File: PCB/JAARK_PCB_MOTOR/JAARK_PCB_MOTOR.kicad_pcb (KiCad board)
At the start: 2 copper layers, 1 part, among them IC1 TPS564242DRLR

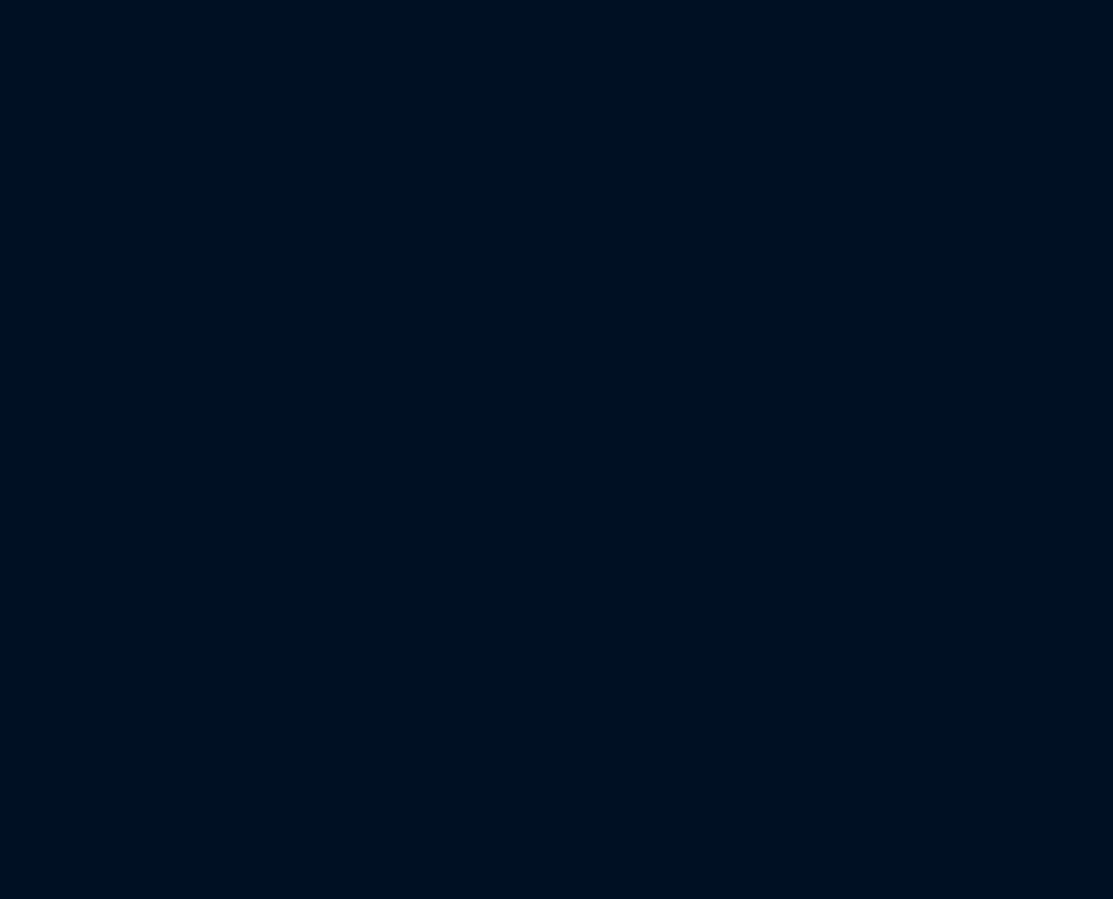
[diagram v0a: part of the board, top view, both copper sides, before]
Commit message: Organizing libraries in the local folder.
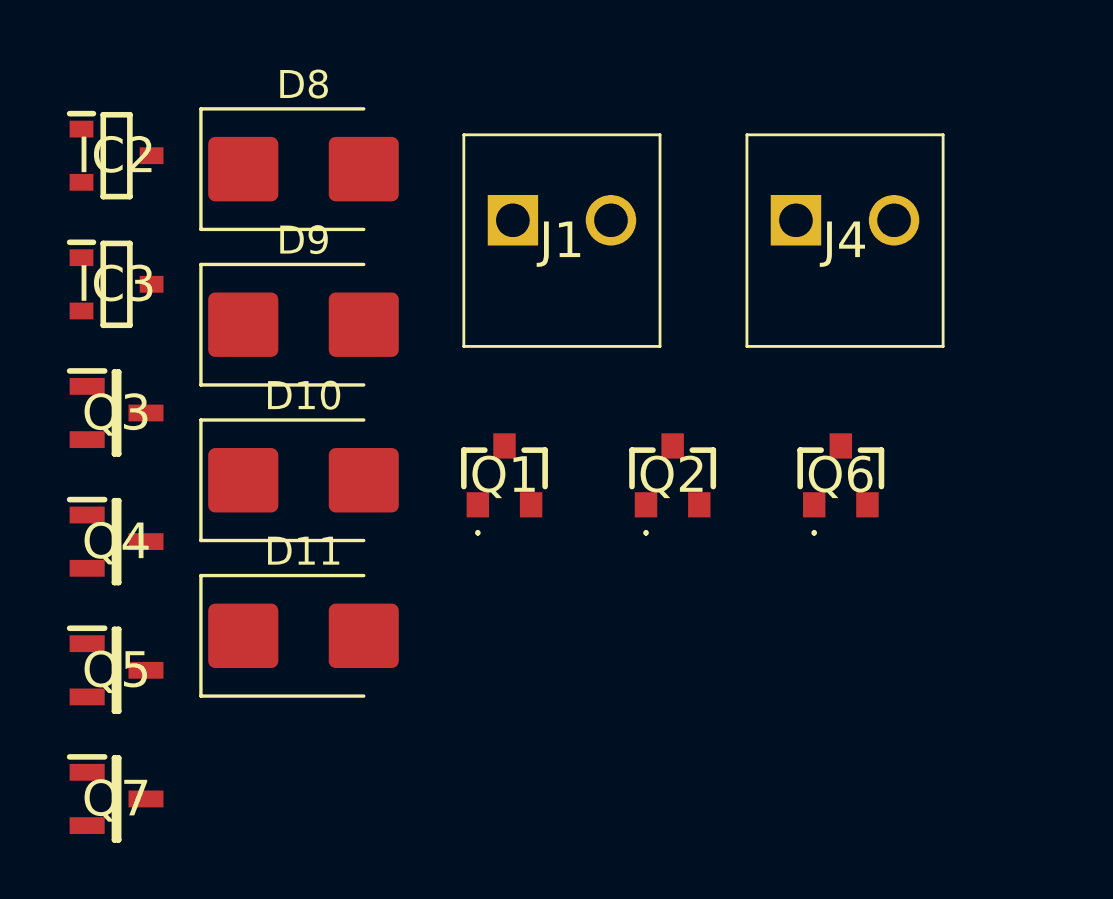
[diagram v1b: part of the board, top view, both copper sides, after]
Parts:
- added D10: S2JTR, Diode_SMD:D_SMB, F.Cu at (66.9, 59.3)
- added D11: S2JTR, Diode_SMD:D_SMB, F.Cu at (66.9, 64.8)
- added D8: S2JTR, Diode_SMD:D_SMB, F.Cu at (66.9, 48.2)
- added D9: S2JTR, Diode_SMD:D_SMB, F.Cu at (66.9, 53.8)
- added IC2: PJA3404_R1_00001, JAARK_lib:SOT95P240X110-3N, F.Cu at (60.2, 47.7)
- added IC3: PJA3404_R1_00001, JAARK_lib:SOT95P240X110-3N, F.Cu at (60.2, 52.3)
- added J1: dc=12, JAARK_lib:1984617, F.Cu at (74.3, 50.0)
- added J4: ~, JAARK_lib:1984617, F.Cu at (84.5, 50.0)
- added Q1: SSM3J334RLF, JAARK_lib:2SC2712GRLF, F.Cu at (74.0, 59.1)
- added Q2: SSM3J334RLF, JAARK_lib:2SC2712GRLF, F.Cu at (80.0, 59.1)
- added Q3: FMMT619TA, JAARK_lib:SOT95P237X112-3N, F.Cu at (60.2, 56.9)
- added Q4: FMMT619TA, JAARK_lib:SOT95P237X112-3N, F.Cu at (60.2, 61.5)
- added Q5: FMMT619TA, JAARK_lib:SOT95P237X112-3N, F.Cu at (60.2, 66.1)
- added Q6: SSM3J334RLF, JAARK_lib:2SC2712GRLF, F.Cu at (86.0, 59.1)
- added Q7: FMMT619TA, JAARK_lib:SOT95P237X112-3N, F.Cu at (60.2, 70.7)
- IC1: footprint SSys_Footprints:SOTFL50P160X60-6N -> JAARK_lib:SOTFL50P160X60-6N

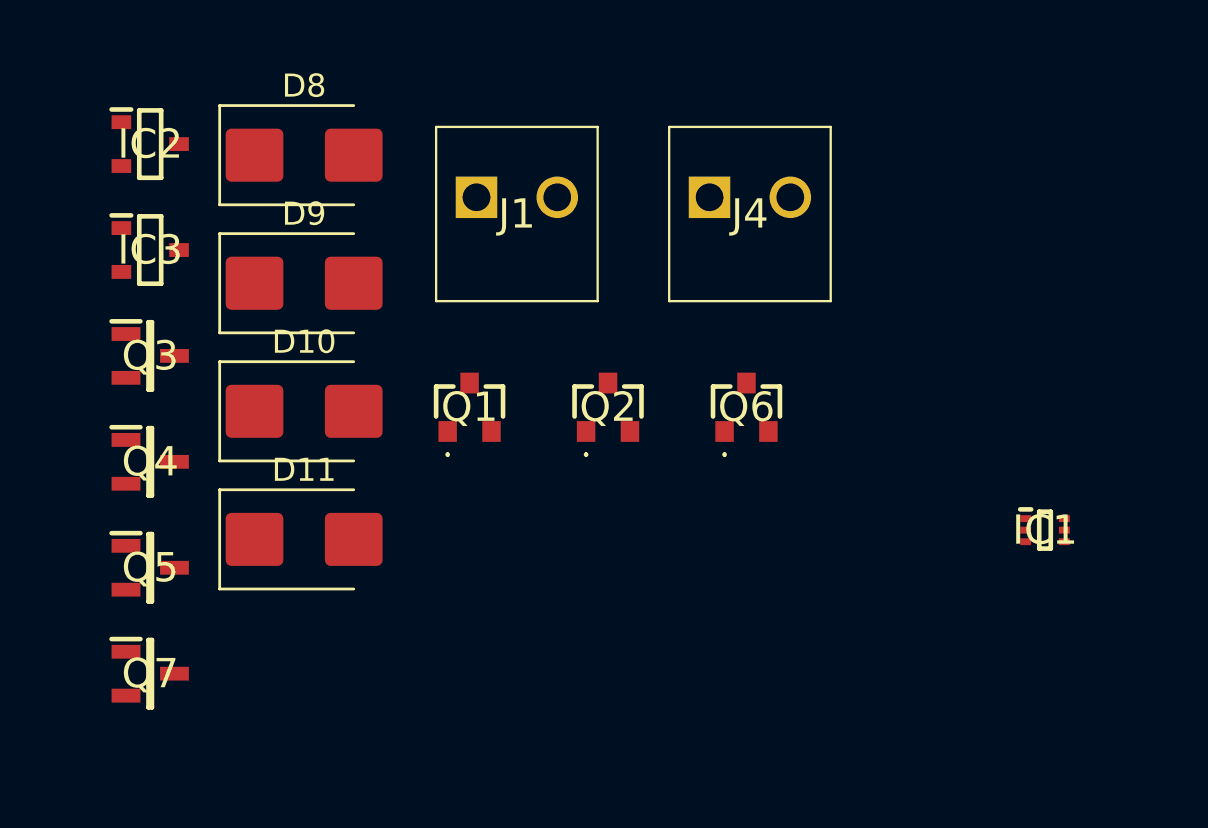
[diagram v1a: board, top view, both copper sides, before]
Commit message: Motor driver recreation, appended footprints to lots of R,L,C elements
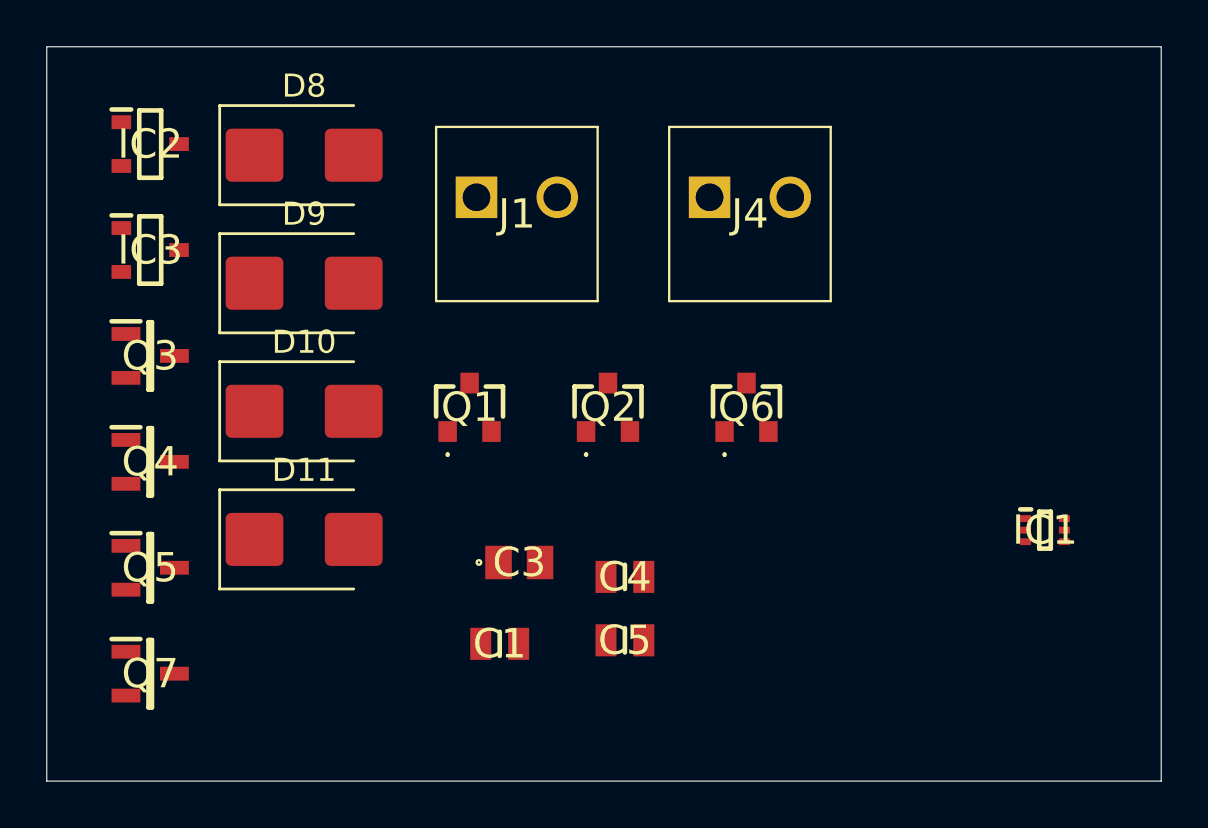
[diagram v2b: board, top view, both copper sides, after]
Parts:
- added C1: 22uF, JAARK_lib:CAPC2012X95N, F.Cu at (75.4, 69.4)
- added C3: 0.1uF, JAARK_lib:C0805, F.Cu at (76.2, 65.8)
- added C4: 22uF, JAARK_lib:CAPC2012X95N, F.Cu at (80.8, 66.5)
- added C5: 22uF, JAARK_lib:CAPC2012X95N, F.Cu at (80.8, 69.2)
- IC2, IC3: footprint JAARK_lib:SOT95P240X110-3N -> SSys_Footprints:SOT95P240X110-3N
- J1, J4: footprint JAARK_lib:1984617 -> SSys_Footprints:1984617
- Q1, Q2, Q6: footprint JAARK_lib:2SC2712GRLF -> SSys_Footprints:2SC2712GRLF
- Q3, Q4, Q5, Q7: footprint JAARK_lib:SOT95P237X112-3N -> SSys_Footprints:SOT95P237X112-3N
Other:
- board outline added: 48.3 x 31.8 mm

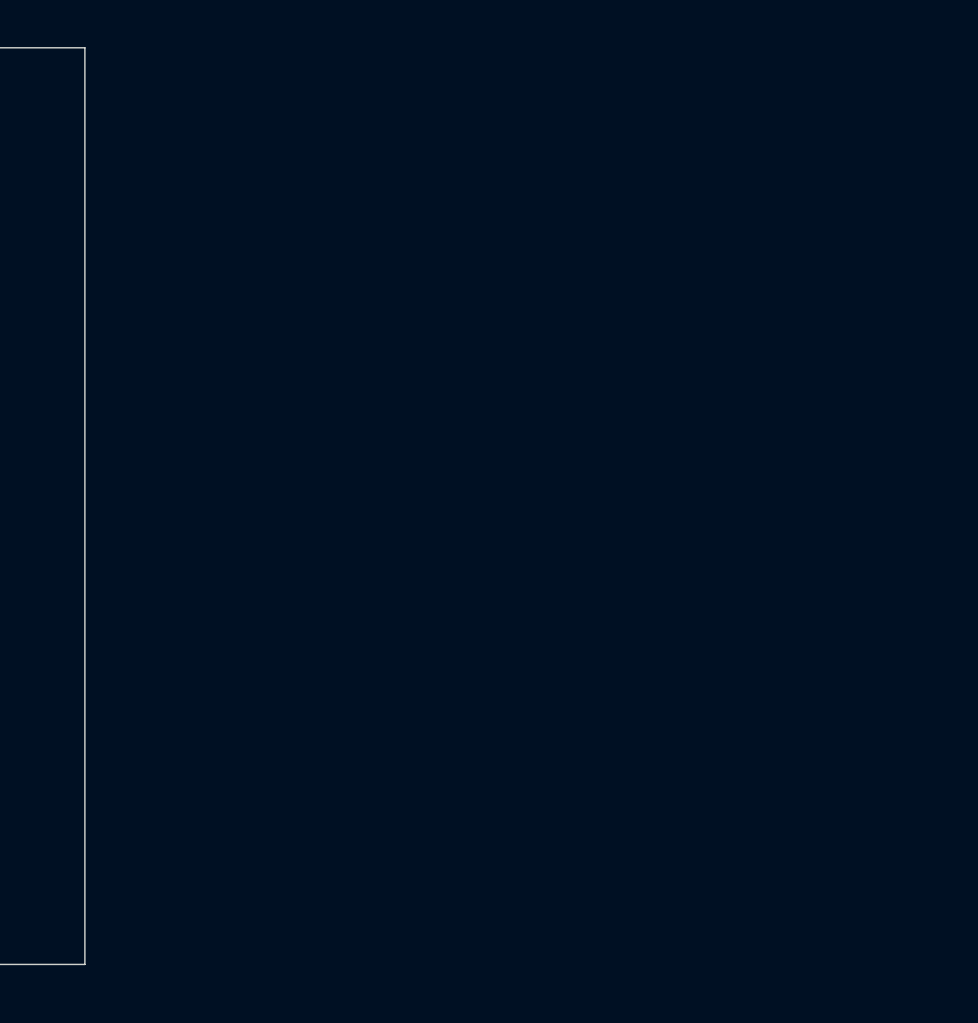
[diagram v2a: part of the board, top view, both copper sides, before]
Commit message: Fixed footprints for sharing
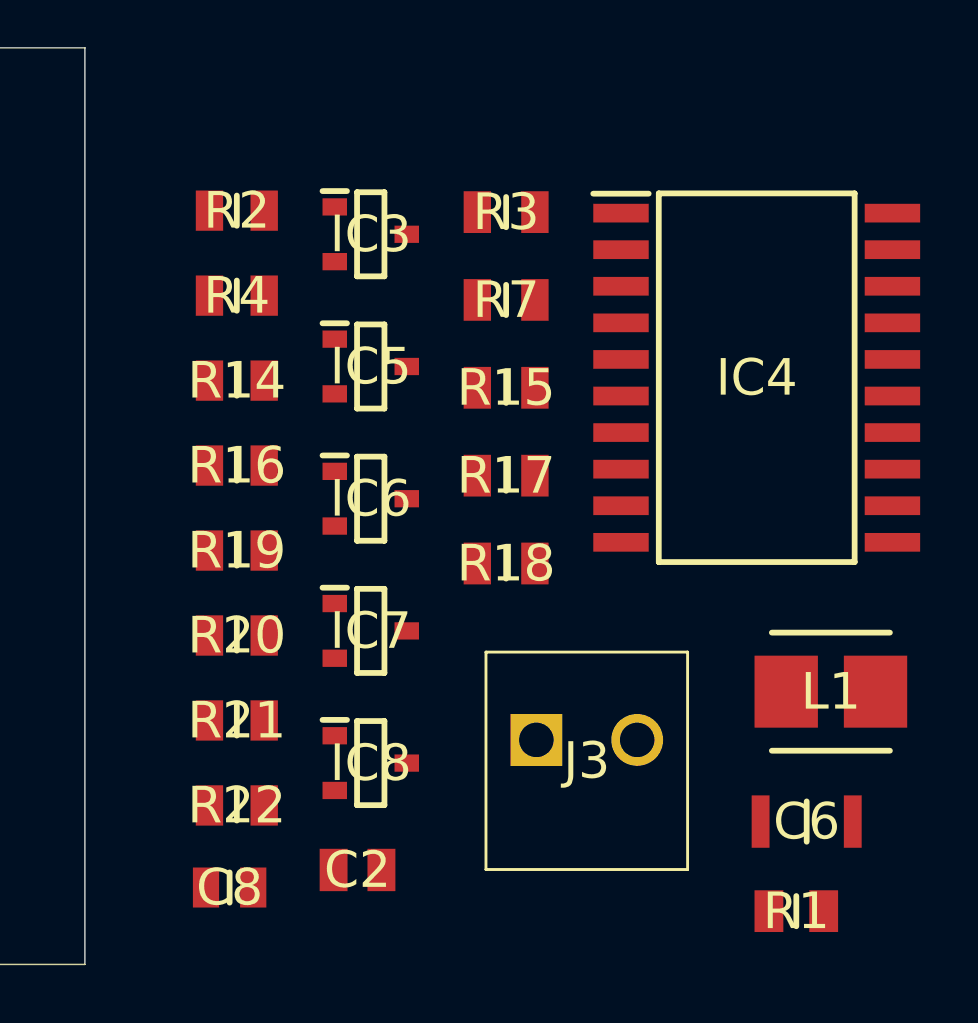
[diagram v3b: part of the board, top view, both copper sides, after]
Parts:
- added C2: 10uF, JAARK_lib:CAPC2012X145N, F.Cu at (113.5, 72.0)
- added C6: 33uF, JAARK_lib:CAPC3216X180N, F.Cu at (129.1, 70.4)
- added C8: 22uF, JAARK_lib:CAPC2012X95N, F.Cu at (109.0, 72.7)
- added IC3: PJA3404_R1_00001, JAARK_lib:SOT95P240X110-3N, F.Cu at (114.0, 50.0)
- added IC4: HIP4080AIBZT, JAARK_lib:SOIC127P1032X265-20N, F.Cu at (127.3, 55.0)
- added IC5: PJA3404_R1_00001, JAARK_lib:SOT95P240X110-3N, F.Cu at (114.0, 54.6)
- added IC6: PJA3404_R1_00001, JAARK_lib:SOT95P240X110-3N, F.Cu at (114.0, 59.2)
- added IC7: PJA3404_R1_00001, JAARK_lib:SOT95P240X110-3N, F.Cu at (114.0, 63.7)
- added IC8: PJA3404_R1_00001, JAARK_lib:SOT95P240X110-3N, F.Cu at (114.0, 68.3)
- added J3: ~, JAARK_lib:1984617, F.Cu at (119.7, 67.5)
- added L1: 1.8uH, JAARK_lib:INDPM4141X200N, F.Cu at (129.9, 65.9)
- added R1: 220kR, JAARK_lib:RESC2012X65N, F.Cu at (128.7, 73.5)
- added R14: 260R, JAARK_lib:RESC2012X60N, F.Cu at (109.3, 55.1)
- added R15: 5kR, JAARK_lib:RESC2012X50N, F.Cu at (118.7, 55.3)
- added R16: 260R, JAARK_lib:RESC2012X60N, F.Cu at (109.3, 58.0)
- added R17: 5kR, JAARK_lib:RESC2012X50N, F.Cu at (118.7, 58.4)
- added R18: 5kR, JAARK_lib:RESC2012X50N, F.Cu at (118.7, 61.4)
- added R19: 10kR, JAARK_lib:RESC2012X60N, F.Cu at (109.3, 61.0)
- added R2: 30kR, JAARK_lib:RESC2012X60N, F.Cu at (109.3, 49.2)
- added R20: 10kR, JAARK_lib:RESC2012X60N, F.Cu at (109.3, 63.9)
- added R21: 260R, JAARK_lib:RESC2012X60N, F.Cu at (109.3, 66.9)
- added R22: 260R, JAARK_lib:RESC2012X60N, F.Cu at (109.3, 69.8)
- added R3: 20kR, JAARK_lib:RESC2012X50N, F.Cu at (118.7, 49.2)
- added R4: 40kR, JAARK_lib:RESC2012X60N, F.Cu at (109.3, 52.1)
- added R7: 5kR, JAARK_lib:RESC2012X50N, F.Cu at (118.7, 52.3)
- IC2: footprint SSys_Footprints:SOT95P240X110-3N -> JAARK_lib:SOT95P240X110-3N
- J1: value dc=12 -> Battery Terminal; footprint SSys_Footprints:1984617 -> JAARK_lib:1984617
- J4: footprint SSys_Footprints:1984617 -> JAARK_lib:1984617
- Q1, Q2, Q6: footprint SSys_Footprints:2SC2712GRLF -> JAARK_lib:2SC2712GRLF
- Q3, Q4, Q5, Q7: footprint SSys_Footprints:SOT95P237X112-3N -> JAARK_lib:SOT95P237X112-3N

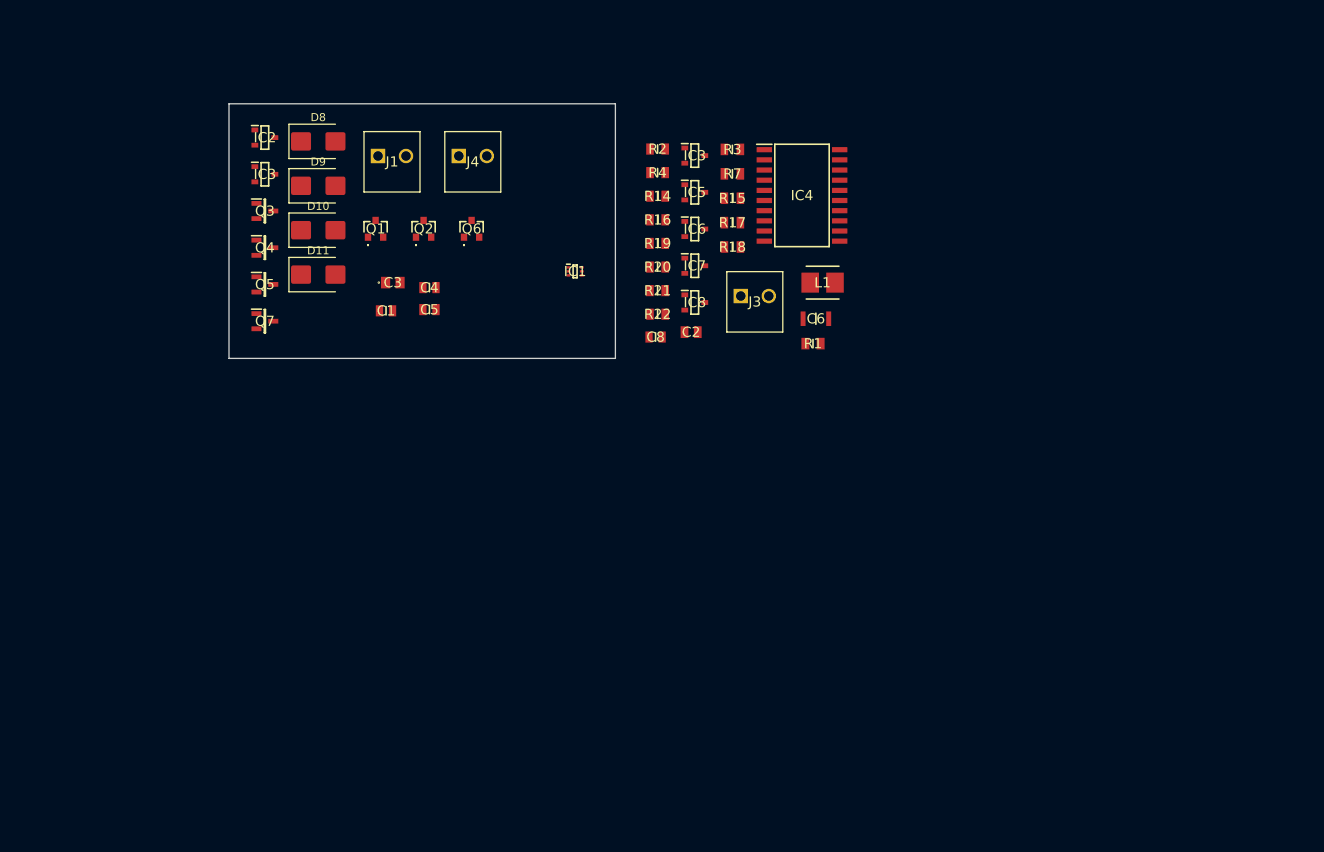
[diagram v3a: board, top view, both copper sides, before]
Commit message: Better motor drivers, fixed capacitor in voltage regulation.
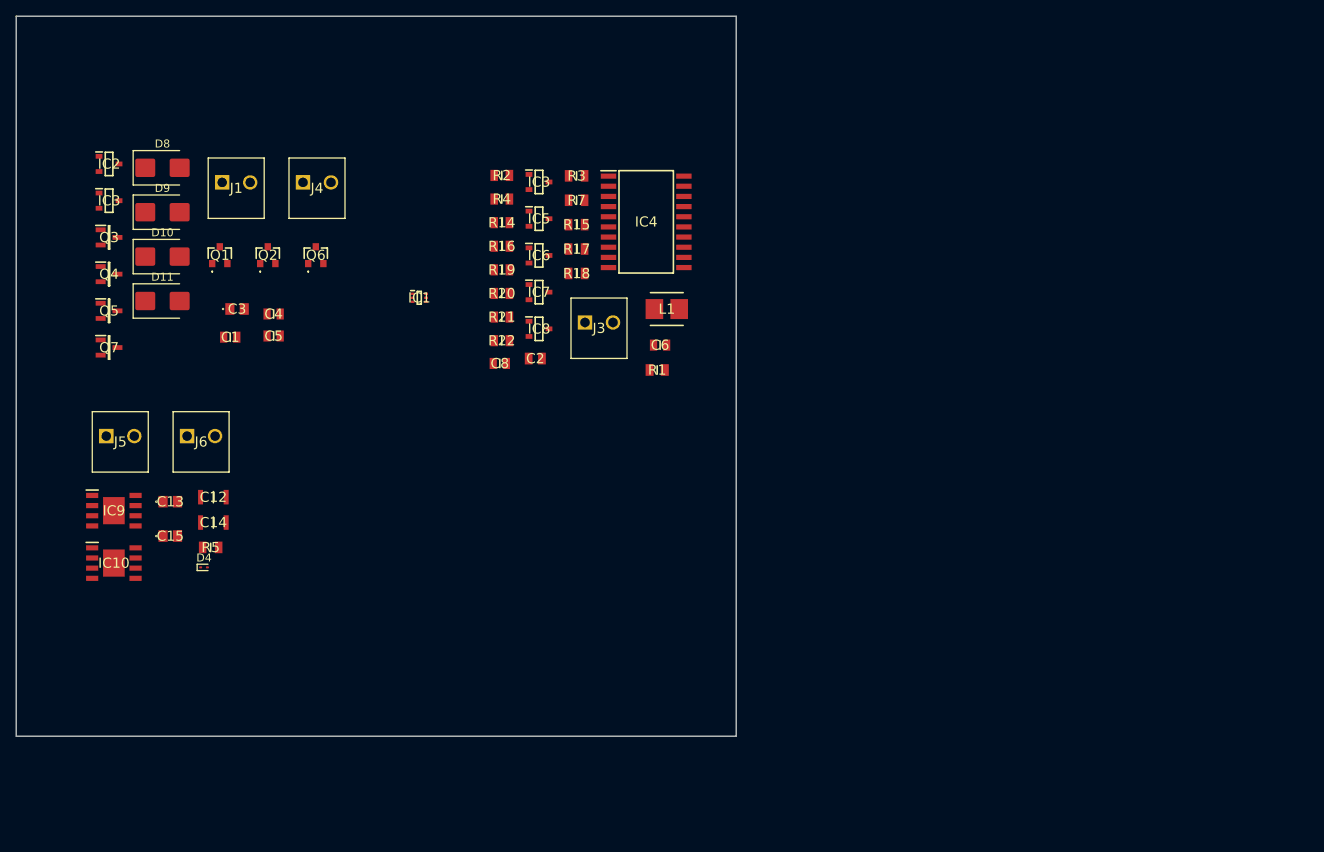
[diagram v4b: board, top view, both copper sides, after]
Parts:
- added C12: 33uF, JAARK_lib:CAPC3216X180N, F.Cu at (53.8, 92.7)
- added C13: 0.1uF, JAARK_lib:C0805, F.Cu at (48.4, 93.2)
- added C14: 33uF, JAARK_lib:CAPC3216X180N, F.Cu at (53.8, 95.8)
- added C15: 0.1uF, JAARK_lib:C0805, F.Cu at (48.4, 97.5)
- added D4: 15V, Diode_SMD:D_SOD-923, F.Cu at (52.6, 101.5)
- added IC10: DRV8231DDAR, JAARK_lib:SOIC127P600X170-9N, F.Cu at (41.3, 100.9)
- added IC9: DRV8231DDAR, JAARK_lib:SOIC127P600X170-9N, F.Cu at (41.3, 94.4)
- added J5: ~, JAARK_lib:1984617, F.Cu at (40.4, 85.0)
- added J6: ~, JAARK_lib:1984617, F.Cu at (50.5, 85.0)
- added R5: 20kR, JAARK_lib:RESC2012X50N, F.Cu at (53.4, 99.0)
- C6: value 33uF -> 220pF; footprint JAARK_lib:CAPC3216X180N -> JAARK_lib:CAPC2012X75N
- moved C6 19.8 mm to (109.6, 73.7)
- moved IC3 19.8 mm to (94.5, 53.3)
- moved IC5 19.8 mm to (94.5, 57.9)
- moved IC6 19.8 mm to (94.5, 62.5)
- moved IC7 19.8 mm to (94.5, 67.0)
- moved IC8 19.8 mm to (94.5, 71.6)
- moved J3 19.8 mm to (100.2, 70.8)
- moved J4 19.8 mm to (65.0, 53.3)
- moved L1 19.8 mm to (110.5, 69.2)
- moved R15 19.8 mm to (99.2, 58.6)
- moved R17 19.8 mm to (99.2, 61.7)
- moved R18 19.8 mm to (99.2, 64.7)
- moved R3 19.8 mm to (99.2, 52.5)
- moved R7 19.8 mm to (99.2, 55.6)
- moved C1 19.8 mm to (55.9, 72.7)
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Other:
- board size 48.3 x 31.8 mm -> 90 x 90 mm
